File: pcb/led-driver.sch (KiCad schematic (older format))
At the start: 13 parts, among them Q201 Q_NMOS_GDSD, Q202 Q_NMOS_GDSD, Q203 Q_NMOS_GDSD, Q204 Q_NMOS_GDSD, U201 LM2902N, U202 MAX5813

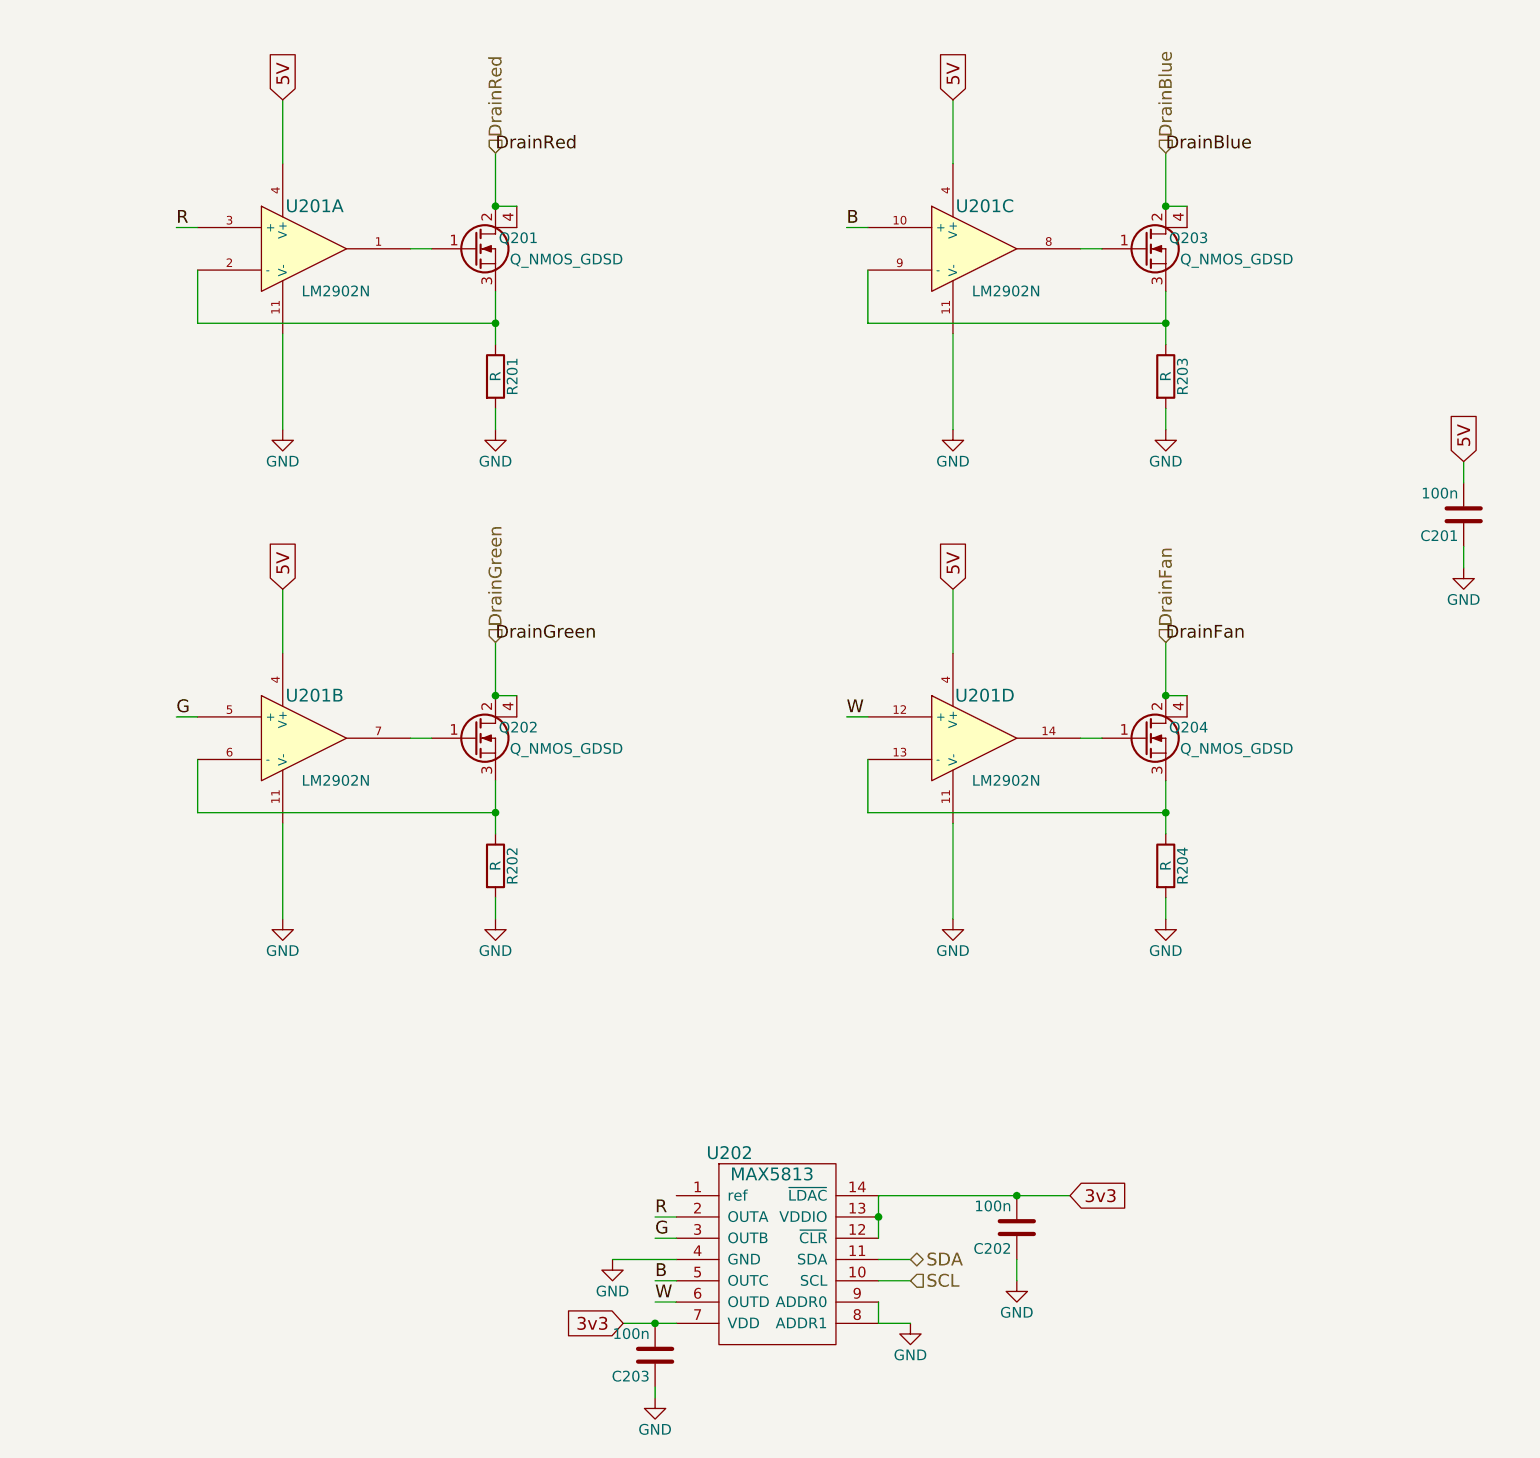
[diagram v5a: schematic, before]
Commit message: added gain to current feedback
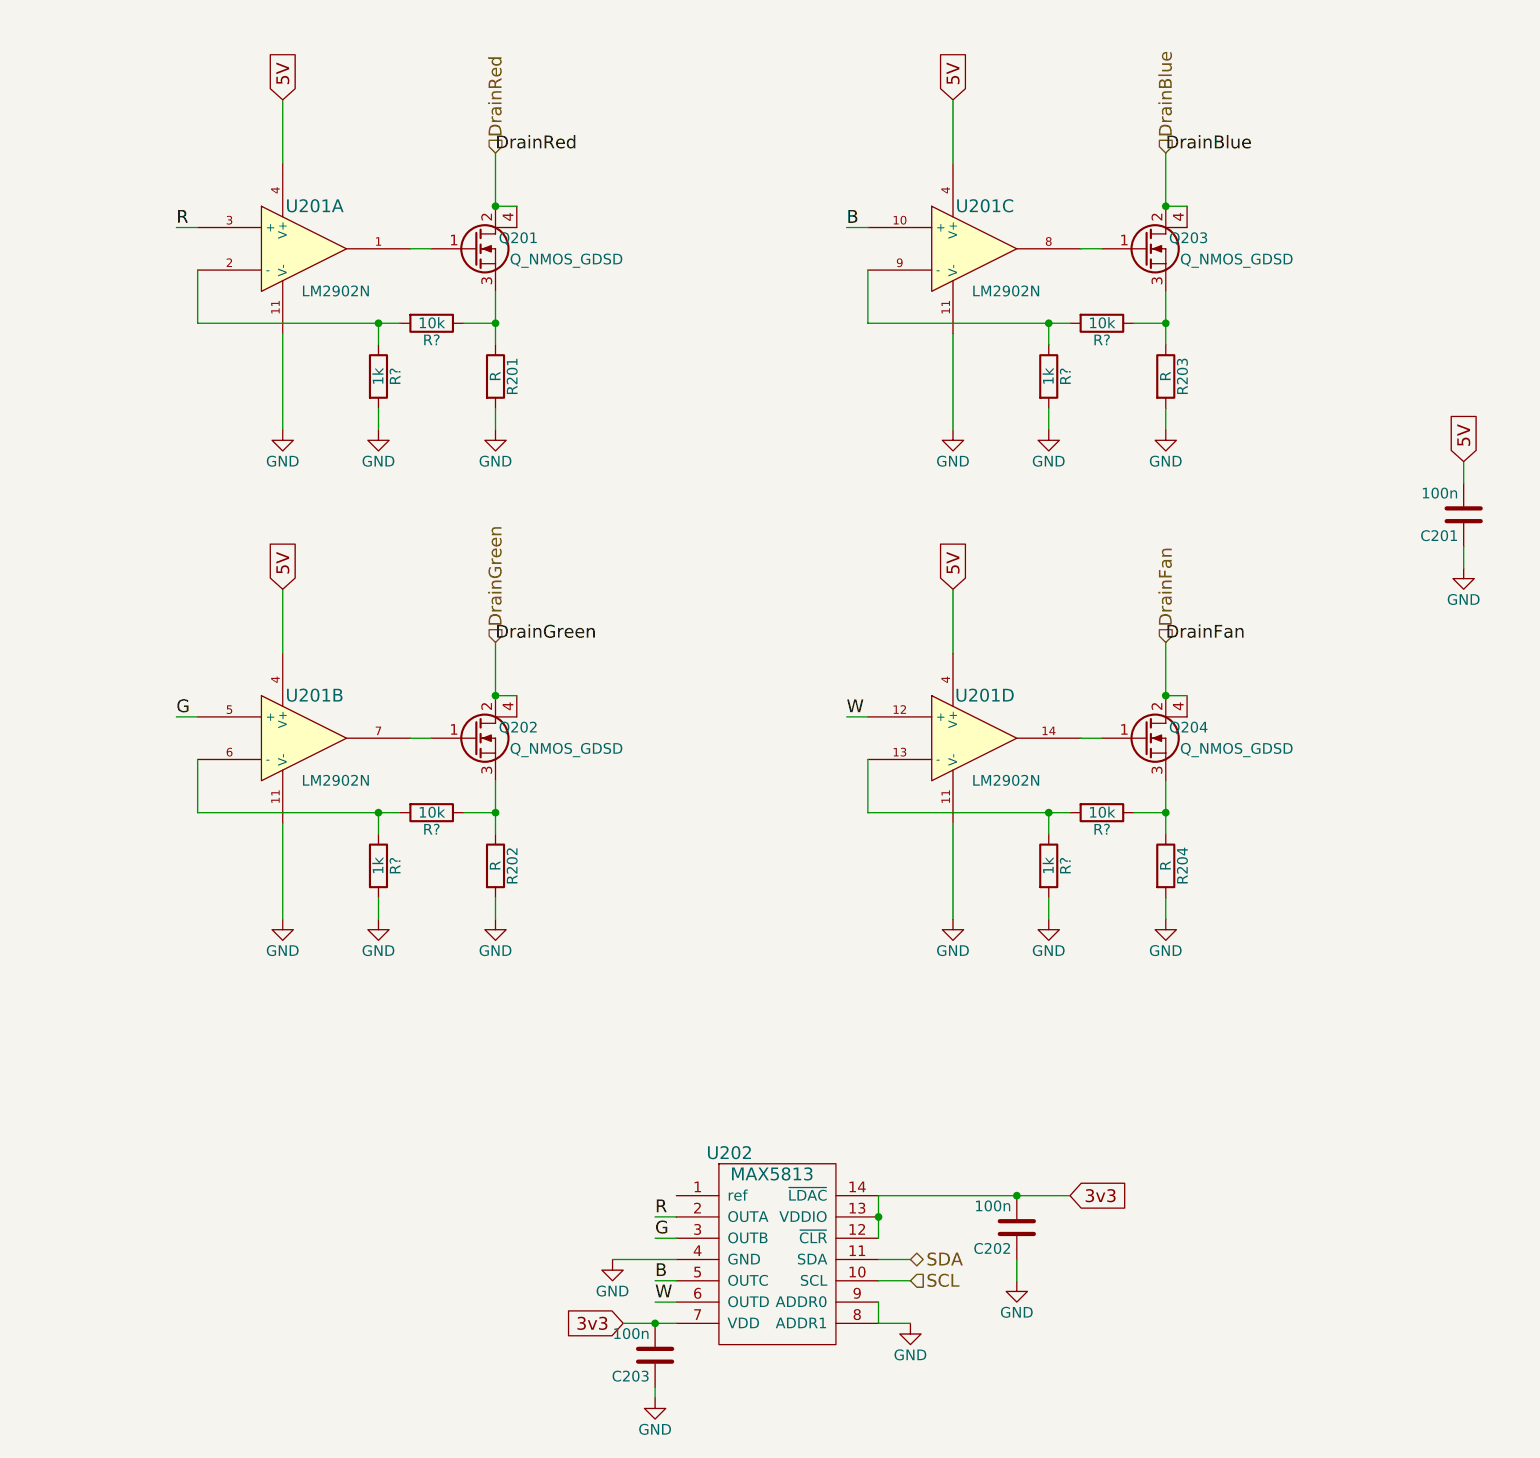
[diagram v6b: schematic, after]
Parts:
- added R? (x4): 1k, symbol R
- added R? (x4): 10k, symbol R
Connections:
- net GND: now also R?.2, R?.2, R?.2, R?.2
- net at Q201.3 (S), R201.1: now also R?.1; no longer U201.2 (-)
- net at Q204.3 (S), R204.1: now also R?.1; no longer U201.13 (-)
- net at Q202.3 (S), R202.1: now also R?.1; no longer U201.6 (-)
- net at Q203.3 (S), R203.1: now also R?.1; no longer U201.9 (-)
- new net: R?.1, R?.2, U201.2 (-)
- new net: R?.1, R?.2, U201.13 (-)
- new net: R?.1, R?.2, U201.6 (-)
- new net: R?.1, R?.2, U201.9 (-)
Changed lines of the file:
@@
 Wire Wire Line
 	3200 1900 3200 2150
-Wire Wire Line
-	1800 2050 1800 1800
 $Comp
 L GND #PWR010
@@
 Wire Wire Line
 	2200 2100 2200 2550
-$Comp
-L LM2902N U201
-U 1 1 566DDC60
-P 2300 1700
-F 0 "U201" H 2350 1900 60  0000 C CNN
-F 1 "LM2902N" H 2450 1500 50  0000 C CNN
-F 2 "Housings_SOIC:SOIC-14_3.9x8.7mm_Pitch1.27mm" H 2300 1700 60  0001 C CNN
-F 3 "" H 2300 1700 60  0000 C CNN
-	1    2300 1700
-	1    0    0    -1
-$EndComp
 Wire Wire Line
 	3200 1250 3200 1500
@@
 	6350 3800 6450 3800
 Connection ~ 6350 3800
-Wire Wire Line
-	4950 4350 6350 4350
 Connection ~ 6350 4350
 Wire Wire Line
@@
 Wire Wire Line
 	2900 4000 2800 4000
-Wire Wire Line
-	1800 4350 3200 4350
 Connection ~ 3200 4350
 Wire Wire Line
 	3200 3800 3300 3800
 Connection ~ 3200 3800
-Wire Wire Line
-	1800 2050 3200 2050
 Connection ~ 3200 2050
 Wire Wire Line
@@
 Wire Wire Line
 	3200 1500 3300 1500
-Wire Wire Line
-	4950 2050 6350 2050
 Wire Wire Line
 	6050 1700 5950 1700
@@
 Text HLabel 6350 3550 1    60   Input ~ 0
 DrainFan
+$Comp
+L R R?
+U 1 1 56C2138A
+P 2650 2300
+F 0 "R?" V 2730 2300 50  0000 C CNN
+F 1 "1k" V 2650 2300 50  0000 C CNN
+F 2 "" V 2580 2300 30  0000 C CNN
+F 3 "" H 2650 2300 30  0000 C CNN
+	1    2650 2300
+	1    0    0    -1
+$EndComp
+$Comp
+L R R?
+U 1 1 56C21412
+P 2900 2050
+F 0 "R?" V 2980 2050 50  0000 C CNN
+F 1 "10k" V 2900 2050 50  0000 C CNN
+F 2 "" V 2830 2050 30  0000 C CNN
+F 3 "" H 2900 2050 30  0000 C CNN
+	1    2900 2050
+	0    1    1    0
+$EndComp
+Wire Wire Line
+	2650 2050 2650 2150
+Wire Wire Line
+	1800 2050 2750 2050
+Connection ~ 2650 2050
+$Comp
+L GND #PWR?
+U 1 1 56C217EC
+P 2650 2550
+F 0 "#PWR?" H 2650 2300 50  0001 C CNN
+F 1 "GND" H 2650 2400 50  0000 C CNN
+F 2 "" H 2650 2550 60  0000 C CNN
+F 3 "" H 2650 2550 60  0000 C CNN
+	1    2650 2550
+	1    0    0    -1
+$EndComp
+Wire Wire Line
+	2650 2450 2650 2550
+$Comp
+L LM2902N U201
+U 1 1 566DDC60
+P 2300 1700
+F 0 "U201" H 2350 1900 60  0000 C CNN
+F 1 "LM2902N" H 2450 1500 50  0000 C CNN
+F 2 "Housings_SOIC:SOIC-14_3.9x8.7mm_Pitch1.27mm" H 2300 1700 60  0001 C CNN
+F 3 "" H 2300 1700 60  0000 C CNN
+	1    2300 1700
+	1    0    0    -1
+$EndComp
+Wire Wire Line
+	1800 1800 1800 2050
+Wire Wire Line
+	3050 2050 3200 2050
+$Comp
+L R R?
+U 1 1 56C21E55
+P 2650 4600
+F 0 "R?" V 2730 4600 50  0000 C CNN
+F 1 "1k" V 2650 4600 50  0000 C CNN
+F 2 "" V 2580 4600 30  0000 C CNN
+F 3 "" H 2650 4600 30  0000 C CNN
+	1    2650 4600
+	1    0    0    -1
+$EndComp
+$Comp
+L GND #PWR?
+U 1 1 56C21E5B
+P 2650 4850
+F 0 "#PWR?" H 2650 4600 50  0001 C CNN
+F 1 "GND" H 2650 4700 50  0000 C CNN
+F 2 "" H 2650 4850 60  0000 C CNN
+F 3 "" H 2650 4850 60  0000 C CNN
+	1    2650 4850
+	1    0    0    -1
+$EndComp
+Wire Wire Line
+	2650 4750 2650 4850
+$Comp
+L R R?
+U 1 1 56C21EB0
+P 2900 4350
+F 0 "R?" V 2980 4350 50  0000 C CNN
+F 1 "10k" V 2900 4350 50  0000 C CNN
+F 2 "" V 2830 4350 30  0000 C CNN
+F 3 "" H 2900 4350 30  0000 C CNN
+	1    2900 4350
+	0    1    1    0
+$EndComp
+Wire Wire Line
+	3200 4350 3050 4350
+Wire Wire Line
+	2750 4350 1800 4350
+Wire Wire Line
+	2650 4450 2650 4350
+Connection ~ 2650 4350
+$Comp
+L R R?
+U 1 1 56C2235C
+P 5800 4600
+F 0 "R?" V 5880 4600 50  0000 C CNN
+F 1 "1k" V 5800 4600 50  0000 C CNN
+F 2 "" V 5730 4600 30  0000 C CNN
+F 3 "" H 5800 4600 30  0000 C CNN
+	1    5800 4600
+	1    0    0    -1
+$EndComp
+$Comp
+L GND #PWR?
+U 1 1 56C22362
+P 5800 4850
+F 0 "#PWR?" H 5800 4600 50  0001 C CNN
+F 1 "GND" H 5800 4700 50  0000 C CNN
+F 2 "" H 5800 4850 60  0000 C CNN
+F 3 "" H 5800 4850 60  0000 C CNN
+	1    5800 4850
+	1    0    0    -1
+$EndComp
+Wire Wire Line
+	5800 4750 5800 4850
+$Comp
+L R R?
+U 1 1 56C22421
+P 6050 4350
+F 0 "R?" V 6130 4350 50  0000 C CNN
+F 1 "10k" V 6050 4350 50  0000 C CNN
+F 2 "" V 5980 4350 30  0000 C CNN
+F 3 "" H 6050 4350 30  0000 C CNN
+	1    6050 4350
+	0    1    1    0
+$EndComp
+Wire Wire Line
+	6350 4350 6200 4350
+Wire Wire Line
+	5900 4350 4950 4350
+Wire Wire Line
+	5800 4450 5800 4350
+Connection ~ 5800 4350
+$Comp
+L R R?
+U 1 1 56C2270D
+P 5800 2300
+F 0 "R?" V 5880 2300 50  0000 C CNN
+F 1 "1k" V 5800 2300 50  0000 C CNN
+F 2 "" V 5730 2300 30  0000 C CNN
+F 3 "" H 5800 2300 30  0000 C CNN
+	1    5800 2300
+	1    0    0    -1
+$EndComp
+$Comp
+L GND #PWR?
+U 1 1 56C22713
+P 5800 2550
+F 0 "#PWR?" H 5800 2300 50  0001 C CNN
+F 1 "GND" H 5800 2400 50  0000 C CNN
+F 2 "" H 5800 2550 60  0000 C CNN
+F 3 "" H 5800 2550 60  0000 C CNN
+	1    5800 2550
+	1    0    0    -1
+$EndComp
+Wire Wire Line
+	5800 2450 5800 2550
+$Comp
+L R R?
+U 1 1 56C22778
+P 6050 2050
+F 0 "R?" V 6130 2050 50  0000 C CNN
+F 1 "10k" V 6050 2050 50  0000 C CNN
+F 2 "" V 5980 2050 30  0000 C CNN
+F 3 "" H 6050 2050 30  0000 C CNN
+	1    6050 2050
+	0    1    1    0
+$EndComp
+Wire Wire Line
+	5800 2150 5800 2050
+Wire Wire Line
+	4950 2050 5900 2050
+Wire Wire Line
+	6200 2050 6350 2050
+Connection ~ 5800 2050
 $EndSCHEMATC

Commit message: added pulldown transistors, moved reference adjust to DAC output
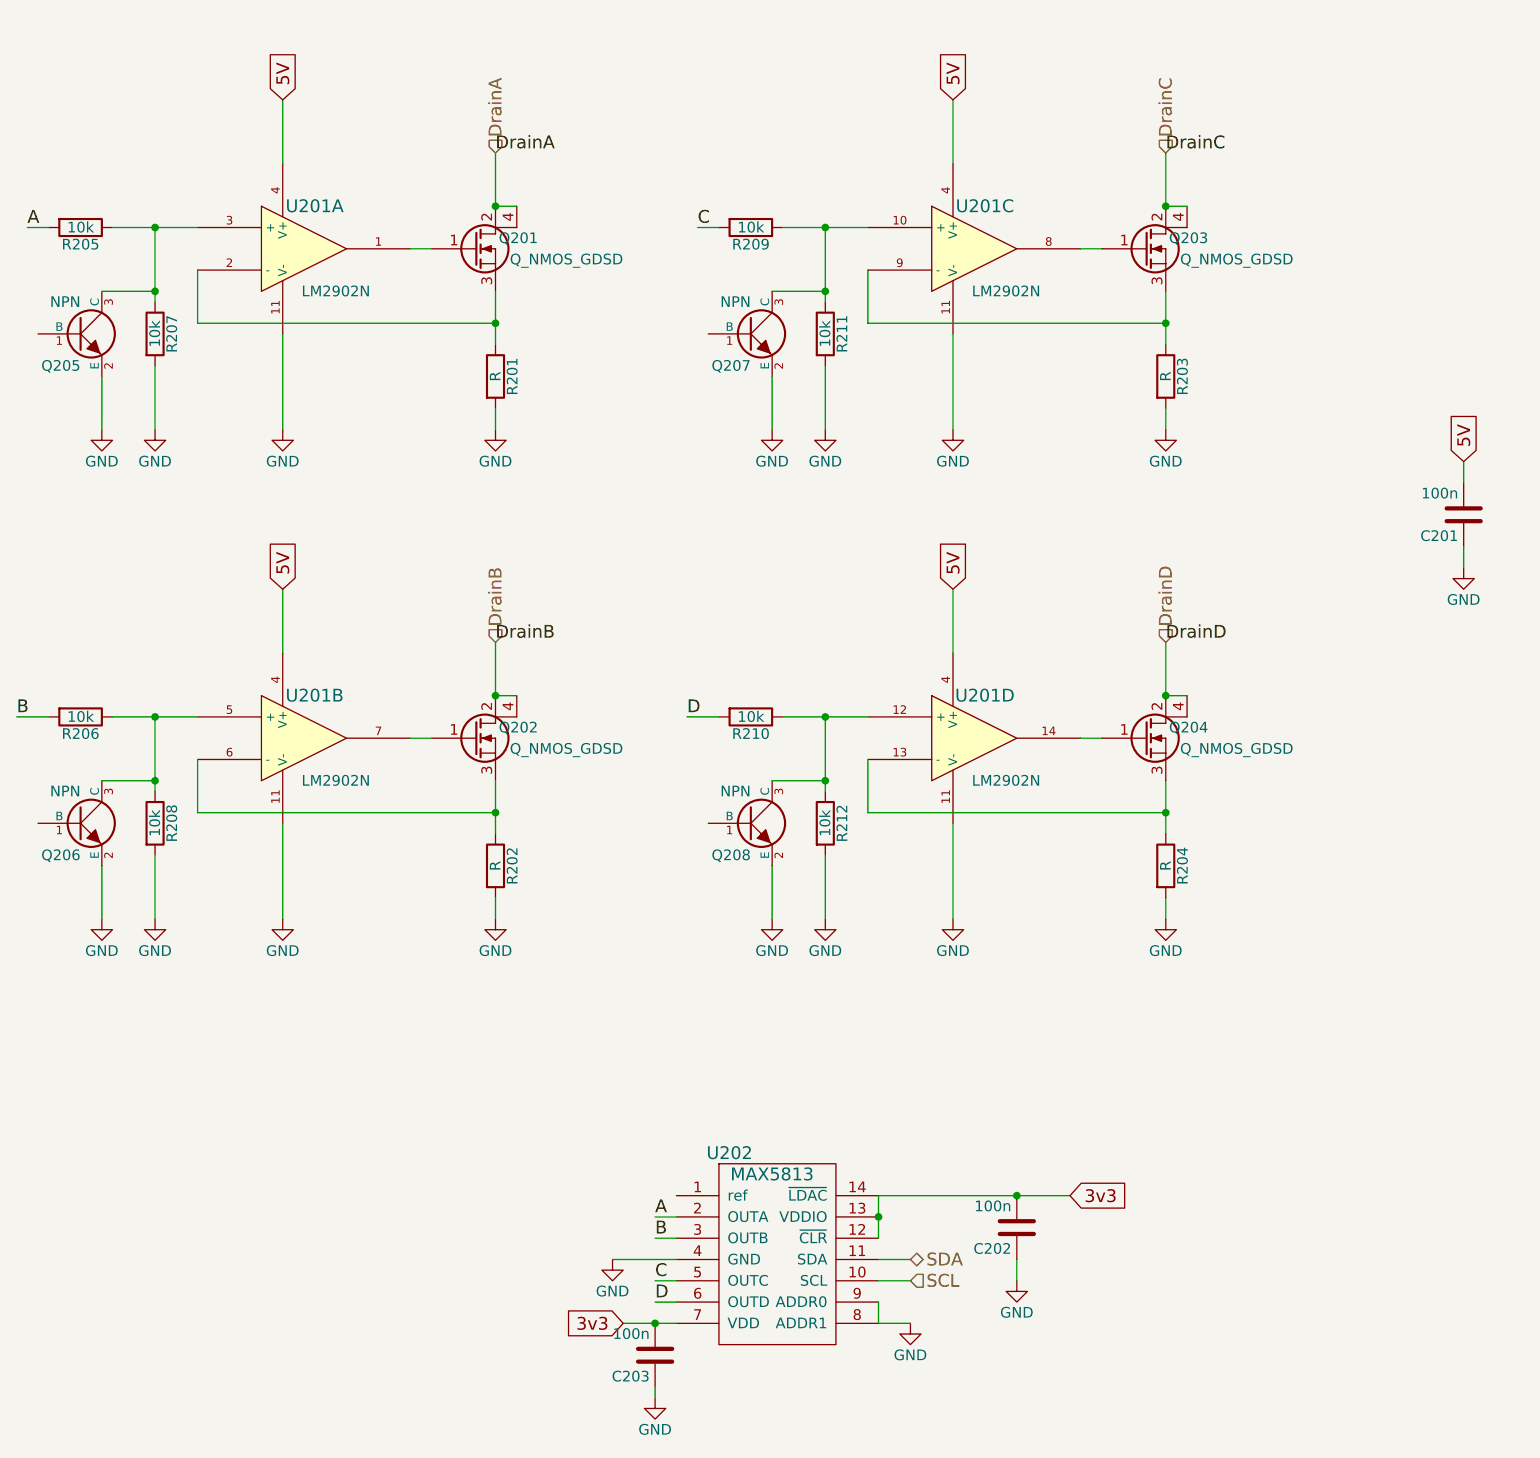
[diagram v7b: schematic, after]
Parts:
- removed R? (x3): 1k, symbol R
- removed R? (x3): 10k, symbol R
- added Q205, Q206, Q207, Q208: NPN, TO_SOT_Packages_SMD:SOT-23, symbol NPN
- added R205, R207, R209, R210, R211, R212: 10k, netl:SMD_0603, symbol R
- R206: renamed from R?; footprint (none) -> netl:SMD_0603
- R208: renamed from R?; value 1k -> 10k; footprint (none) -> netl:SMD_0603
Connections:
- net B: now also R206.2, U202.3 (OUTB); no longer U201.10 (+), U202.5 (OUTC)
- net GND: now also Q205.2 (E), Q206.2 (E), Q207.2 (E), Q208.2 (E), R207.2, R211.2, R212.2
- net at U201.2 (-): now also Q201.3 (S), R201.1
- net at Q204.3 (S), R204.1: now also U201.13 (-)
- net at Q202.3 (S), R202.1: now also U201.6 (-); no longer R206.1
- net at Q203.3 (S), R203.1: now also U201.9 (-)
- net DrainBlue renamed DrainC
- net DrainFan renamed DrainD
- net DrainGreen renamed DrainB
- net DrainRed renamed DrainA
- net G: no longer names the net of U201.5 (+)
- net G: now also R206.1, R208.1, Q206.3 (C); no longer U202.3 (OUTB)
- net R: no longer names the net of U201.3 (+)
- net R: now also Q205.3 (C), R205.1, R207.1; no longer U202.2 (OUTA)
- net W: no longer names the net of U201.12 (+)
- net W: now also Q208.3 (C), R210.1, R212.1; no longer U202.6 (OUTD)
- new net: Q207.3 (C), R209.1, R211.1, U201.10 (+)
- new net A: R205.2, U202.2 (OUTA)
- new net C: R209.2, U202.5 (OUTC)
- new net D: R210.2, U202.6 (OUTD)
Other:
- moved on the sheet: R206, R208

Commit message: starting to work on adding the mcu
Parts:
- added R213, R214, R215, R216, R217, R218, R219, R220: R, symbol R
- U201: symbol LM2902N -> LM2902N-RESCUE-rpi_shield
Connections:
- net at U201.1: now also R215.2; no longer Q201.1 (G)
- net at R205.1, R207.1, U201.3 (+): no longer Q205.3 (C)
- net at R210.1, R212.1, U201.12 (+): no longer Q208.3 (C)
- net at U201.14: now also R220.2; no longer Q204.1 (G)
- net at R206.1, R208.1, U201.5 (+): no longer Q206.3 (C)
- net at U201.7: now also R216.2; no longer Q202.1 (G)
- net at R209.1, R211.1, U201.10 (+): no longer Q207.3 (C)
- net at U201.8: now also R219.2; no longer Q203.1 (G)
- net at Q208.1 (B): now also R218.1
- net at Q206.1 (B): now also R214.1
- net at Q205.1 (B): now also R213.1
- net at Q207.1 (B): now also R217.1
- new net: Q202.1 (G), Q206.3 (C), R216.1
- new net: Q201.1 (G), Q205.3 (C), R215.1
- new net: Q204.1 (G), Q208.3 (C), R220.1
- new net: Q203.1 (G), Q207.3 (C), R219.1
- new net PWMA: R213.2
- new net PWMB: R214.2
- new net PWMC: R217.2
- new net PWMD: R218.2
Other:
- moved on the sheet: Q201, Q202, Q203, Q204, Q205, Q206, Q207, Q208, R201, R202, R203, R204
